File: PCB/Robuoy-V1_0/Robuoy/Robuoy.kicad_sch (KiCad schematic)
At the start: 6 parts

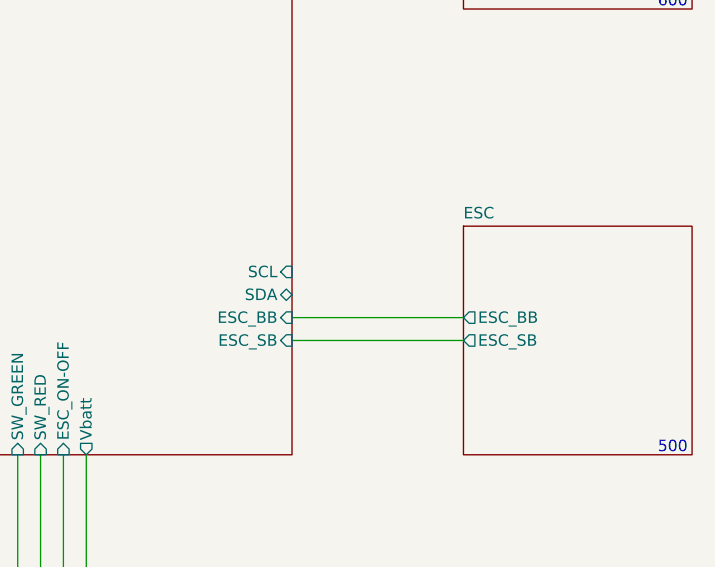
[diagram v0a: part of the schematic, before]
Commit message: Schematics changed for new design
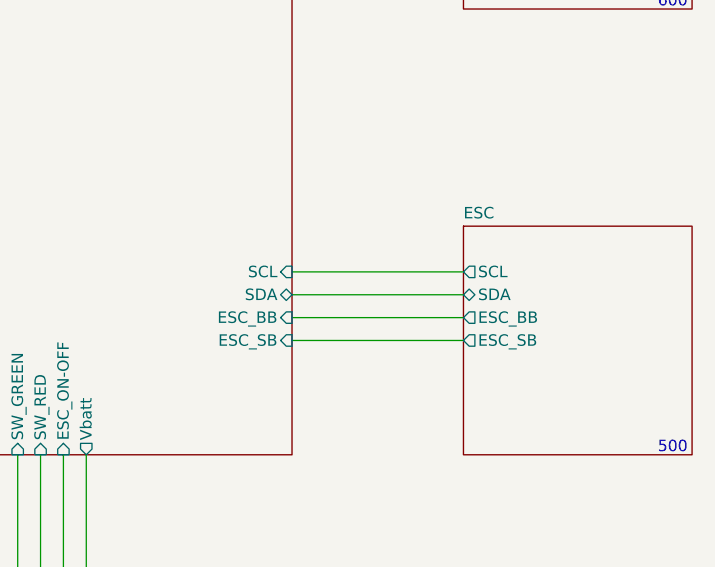
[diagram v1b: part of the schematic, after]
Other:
- sheet ESC ports: added SCL, SDA; removed none
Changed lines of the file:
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@@
 	(wire
 		(pts
+			(xy 139.7 100.33) (xy 158.75 100.33)
+		)
+		(stroke
+			(width 0)
+			(type default)
+		)
+	)
+	(wire
+		(pts
 			(xy 111.76 120.65) (xy 111.76 161.29)
 		)
@@
 		(pts
 			(xy 109.22 120.65) (xy 109.22 161.29)
+		)
+		(stroke
+			(width 0)
+			(type default)
+		)
+	)
+	(wire
+		(pts
+			(xy 139.7 102.87) (xy 158.75 102.87)
 		)
 		(stroke
@@
 			(effects
 				(font
+					(size 1.27 1.27)
+				)
+				(justify left)
+			)
+		)
+		(pin "SCL" output
+			(at 158.75 100.33 180)
+			(effects
+				(font
+					(size 1.27 1.27)
+				)
+				(justify left)
+			)
+		)
+		(pin "SDA" bidirectional
+			(at 158.75 102.87 180)
+			(effects
+				(font
